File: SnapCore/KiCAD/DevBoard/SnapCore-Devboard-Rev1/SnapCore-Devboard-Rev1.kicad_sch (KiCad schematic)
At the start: 56 parts, among them J2 USB_C_Receptacle_USB2.0_16P, J3 Conn_01x18_Pin, Q1 AO3407A, SW2 TS-1187A, U1 nRF52840-QIXX, U2 XC6220B331MR, U5 TP4056-42-ESOP8, Y1 32.768KHz, Y2 32MHz

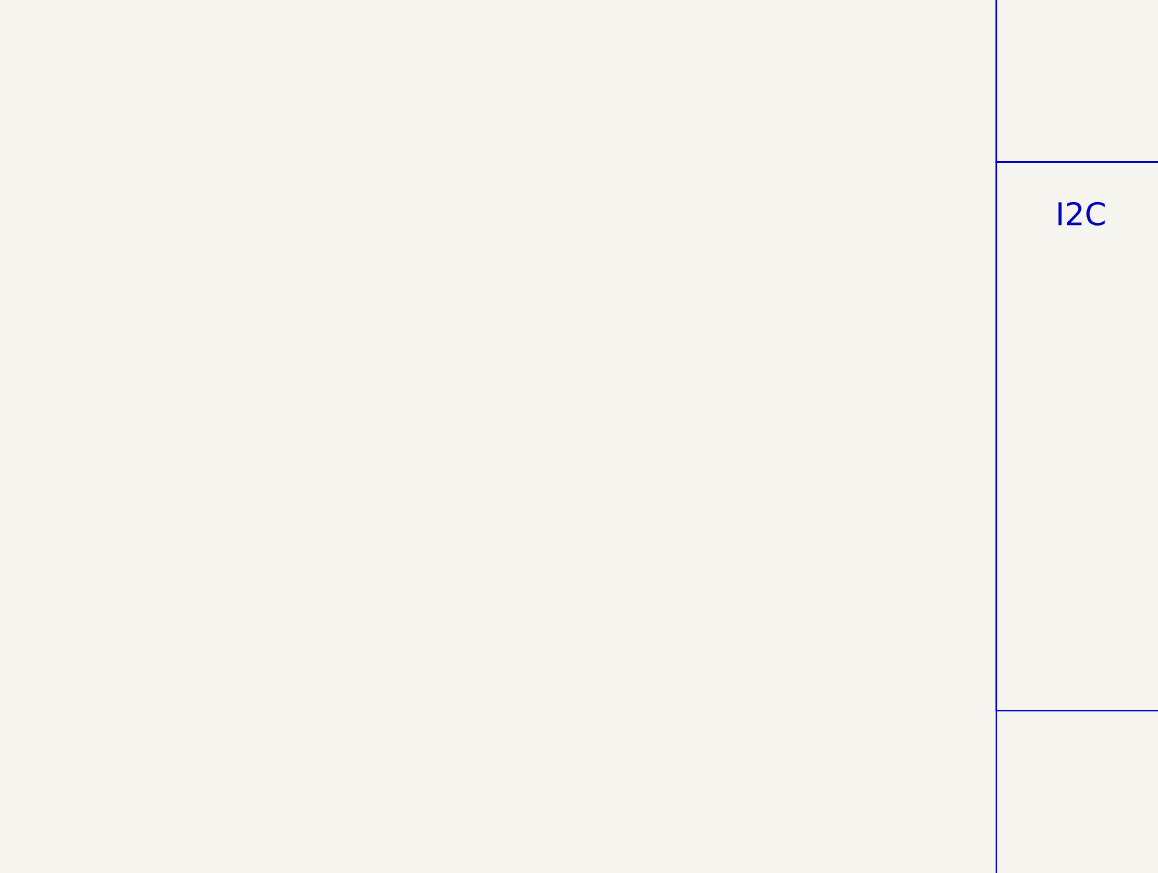
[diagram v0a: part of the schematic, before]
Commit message: Tried implementing AS5600 on the board
Added schematic
Need to rework layout first to integrate properly (or use breakout board instead)
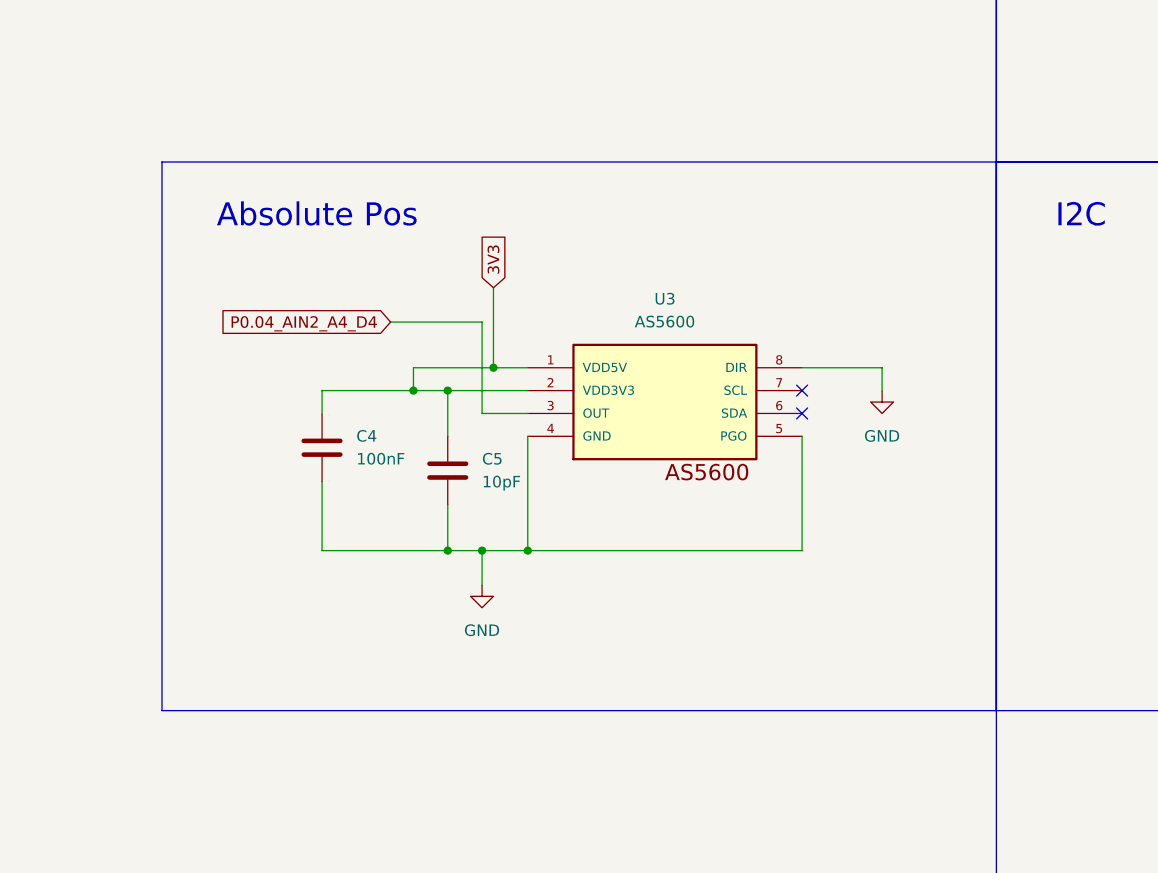
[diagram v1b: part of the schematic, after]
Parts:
- added C4: 100nF, Capacitor_SMD:C_0402_1005Metric, symbol Device:C
- added C5: 10pF, Capacitor_SMD:C_0402_1005Metric, symbol Device:C
- added U3: AS5600, AS5600:SOIC8, symbol AS5600:AS5600
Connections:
- net 3V3: now also C4.1, C5.1, U3.1 (VDD5V), U3.2 (VDD3V3)
- net GND: now also C4.2, C5.2, U3.4 (GND), U3.5 (PGO), U3.8 (DIR)
- net P0.04_AIN2_A4_D4: now also U3.3 (OUT)
- no-connect marks 24 -> 26
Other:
- note added: "Absolute Pos"
